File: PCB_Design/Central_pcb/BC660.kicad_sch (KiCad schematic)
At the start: 26 parts, among them J1 SMA_CONNECTOR, J2 Conn_01x01_Pin, J3 Conn_01x02_Pin, J4 SIM8051-6-0-14-01-X-REVD, J5 Conn_01x02_Pin, J6 Conn_01x06_Pin, U1 BC660K-GL, U2 ESDS304DBVR

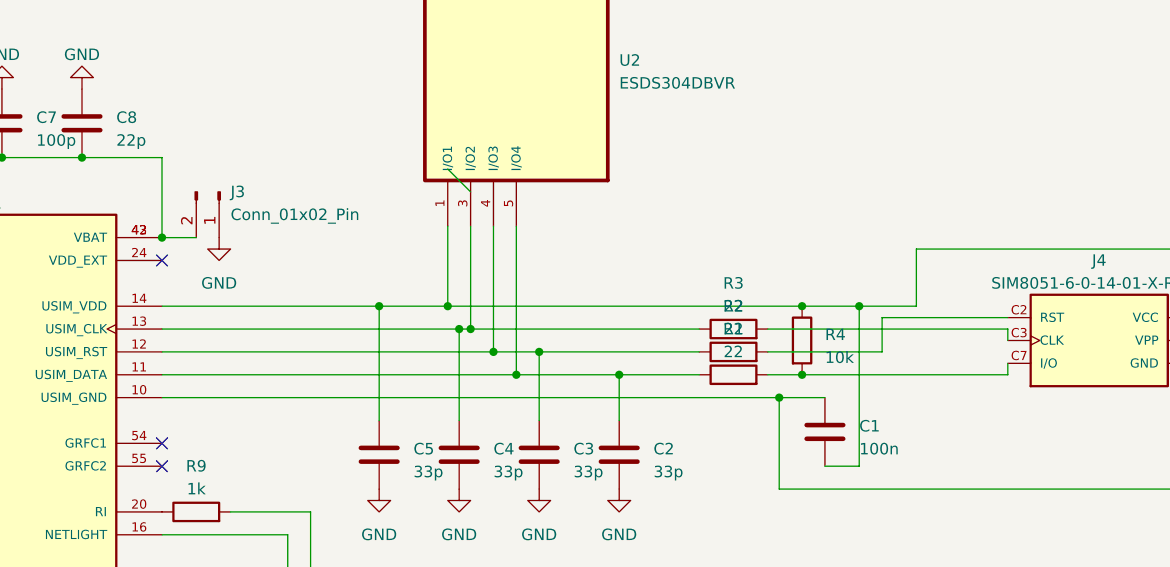
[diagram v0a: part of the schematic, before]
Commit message: Power part added
Power part is finished with power footprints
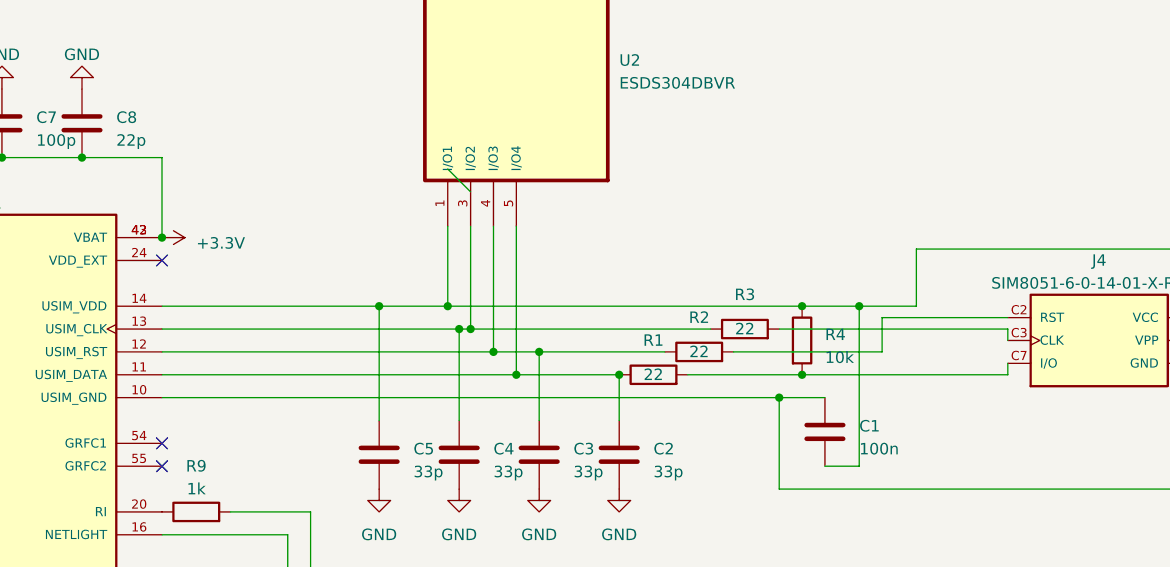
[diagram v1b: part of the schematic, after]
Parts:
- removed J3: Conn_01x02_Pin, Connector_PinHeader_2.54mm:PinHeader_1x02_P2.54mm_Vertical, symbol Connector:Conn_01x02_Pin
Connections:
- net +3.3V: now reaches C6.2, C7.2, C8.2, C9.2, U1.42 (VBAT), U1.43 (VBAT)
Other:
- moved on the sheet: R1, R2, R3
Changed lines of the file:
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@@
   (junction (at 124.46 66.04) (diameter 0) (color 0 0 0 0)
   )
+  (junction (at 184.15 90.17) (diameter 0) (color 0 0 0 0)
+  )
+  (junction (at 166.37 85.09) (diameter 0) (color 0 0 0 0)
+  )
+  (junction (at 175.26 87.63) (diameter 0) (color 0 0 0 0)
+  )
+  (junction (at 210.82 82.55) (diameter 0) (color 0 0 0 0)
+  )
+  (junction (at 165.1 82.55) (diameter 0) (color 0 0 0 0)
+  )
   (junction (at 133.35 74.93) (diameter 0) (color 0 0 0 0)
-  )
-  (junction (at 184.15 90.17) (diameter 0) (color 0 0 0 0)
-  )
-  (junction (at 166.37 85.09) (diameter 0) (color 0 0 0 0)
-  )
-  (junction (at 175.26 87.63) (diameter 0) (color 0 0 0 0)
-  )
-  (junction (at 210.82 82.55) (diameter 0) (color 0 0 0 0)
-  )
-  (junction (at 165.1 82.55) (diameter 0) (color 0 0 0 0)
   )
   (junction (at 167.64 85.09) (diameter 0) (color 0 0 0 0)
@@
     (stroke (width 0) (type default))
   )
-  (wire (pts (xy 133.35 74.93) (xy 137.16 74.93))
-    (stroke (width 0) (type default))
-  )
   (wire (pts (xy 58.42 97.79) (xy 53.34 97.79))
     (stroke (width 0) (type default))
@@
     (stroke (width 0) (type default))
   )
-  (wire (pts (xy 200.66 90.17) (xy 204.47 90.17))
+  (wire (pts (xy 191.77 90.17) (xy 204.47 90.17))
     (stroke (width 0) (type default))
   )
@@
     (stroke (width 0) (type default))
   )
-  (wire (pts (xy 167.64 85.09) (xy 193.04 85.09))
+  (wire (pts (xy 167.64 85.09) (xy 194.31 85.09))
     (stroke (width 0) (type default))
   )
@@
     (stroke (width 0) (type default))
   )
-  (wire (pts (xy 200.66 85.09) (xy 227.33 85.09))
+  (wire (pts (xy 201.93 85.09) (xy 227.33 85.09))
     (stroke (width 0) (type default))
   )
@@
     (stroke (width 0) (type default))
   )
-  (wire (pts (xy 200.66 87.63) (xy 213.36 87.63))
+  (wire (pts (xy 196.85 87.63) (xy 213.36 87.63))
     (stroke (width 0) (type default))
   )
@@
     (stroke (width 0) (type default))
   )
-  (wire (pts (xy 184.15 90.17) (xy 193.04 90.17))
-    (stroke (width 0) (type default))
-  )
   (wire (pts (xy 53.34 102.87) (xy 73.66 102.87))
     (stroke (width 0) (type default))
@@
     (stroke (width 0) (type default))
   )
-  (wire (pts (xy 175.26 87.63) (xy 193.04 87.63))
+  (wire (pts (xy 175.26 87.63) (xy 189.23 87.63))
     (stroke (width 0) (type default))
   )
@@
     )
   )
-  (symbol (lib_id "Device:R") (at 196.85 85.09 90) (unit 1)
-    (in_bom yes) (on_board yes) (dnp no) (fields_autoplaced)
-    (property "Reference" "R3" (at 196.85 80.01 90)
-      (effects (font (size 1.27 1.27)))
-    )
-    (property "Value" "22" (at 196.85 82.55 90)
-      (effects (font (size 1.27 1.27)))
-    )
-    (property "Footprint" "Resistor_SMD:R_0805_2012Metric_Pad1.20x1.40mm_HandSolder" (at 196.85 86.868 90)
-      (effects (font (size 1.27 1.27)) hide)
-    )
-    (property "Datasheet" "~" (at 196.85 85.09 0)
+  (symbol (lib_id "Device:R") (at 198.12 85.09 90) (unit 1)
+    (in_bom yes) (on_board yes) (dnp no)
+    (property "Reference" "R3" (at 198.12 81.28 90)
+      (effects (font (size 1.27 1.27)))
+    )
+    (property "Value" "22" (at 198.12 85.09 90)
+      (effects (font (size 1.27 1.27)))
+    )
+    (property "Footprint" "Resistor_SMD:R_0805_2012Metric_Pad1.20x1.40mm_HandSolder" (at 198.12 86.868 90)
+      (effects (font (size 1.27 1.27)) hide)
+    )
+    (property "Datasheet" "~" (at 198.12 85.09 0)
       (effects (font (size 1.27 1.27)) hide)
     )
@@
         (path "/d627ecd8-d3ea-468a-86f8-a115d49eee0e"
           (reference "C2") (unit 1)
-        )
-      )
-    )
-  )
-  (symbol (lib_id "power:GND") (at 139.7 74.93 0) (unit 1)
-    (in_bom yes) (on_board yes) (dnp no) (fields_autoplaced)
-    (property "Reference" "#PWR08" (at 139.7 81.28 0)
-      (effects (font (size 1.27 1.27)) hide)
-    )
-    (property "Value" "GND" (at 139.7 80.01 0)
-      (effects (font (size 1.27 1.27)))
-    )
-    (property "Footprint" "" (at 139.7 74.93 0)
-      (effects (font (size 1.27 1.27)) hide)
-    )
-    (property "Datasheet" "" (at 139.7 74.93 0)
-      (effects (font (size 1.27 1.27)) hide)
-    )
-    (pin "1")
-    (instances
-      (project "Central_pcb"
-        (path "/4d244925-fc91-48ed-8daa-e4f0d6afeb7f"
-          (reference "#PWR08") (unit 1)
-        )
-        (path "/4d244925-fc91-48ed-8daa-e4f0d6afeb7f/a01f4f1b-67d6-4452-bfd1-ae36b9ad65e8"
-          (reference "#PWR08") (unit 1)
-        )
-      )
-      (project "bc660_breakoutboard"
-        (path "/d627ecd8-d3ea-468a-86f8-a115d49eee0e"
-          (reference "#PWR08") (unit 1)
         )
       )
@@
     )
   )
+  (symbol (lib_id "power:+3.3V") (at 133.35 74.93 270) (unit 1)
+    (in_bom yes) (on_board yes) (dnp no) (fields_autoplaced)
+    (property "Reference" "#PWR08" (at 129.54 74.93 0)
+      (effects (font (size 1.27 1.27)) hide)
+    )
+    (property "Value" "+3.3V" (at 137.16 75.565 90)
+      (effects (font (size 1.27 1.27)) (justify left))
+    )
+    (property "Footprint" "" (at 133.35 74.93 0)
+      (effects (font (size 1.27 1.27)) hide)
+    )
+    (property "Datasheet" "" (at 133.35 74.93 0)
+      (effects (font (size 1.27 1.27)) hide)
+    )
+    (pin "1")
+    (instances
+      (project "Central_pcb"
+        (path "/4d244925-fc91-48ed-8daa-e4f0d6afeb7f/a01f4f1b-67d6-4452-bfd1-ae36b9ad65e8"
+          (reference "#PWR08") (unit 1)
+        )
+      )
+    )
+  )
   (symbol (lib_id "power:GND") (at 97.79 58.42 180) (unit 1)
     (in_bom yes) (on_board yes) (dnp no) (fields_autoplaced)
@@
     )
   )
-  (symbol (lib_id "Device:R") (at 196.85 90.17 90) (unit 1)
-    (in_bom yes) (on_board yes) (dnp no) (fields_autoplaced)
-    (property "Reference" "R1" (at 196.85 85.09 90)
-      (effects (font (size 1.27 1.27)))
-    )
-    (property "Value" "22" (at 196.85 87.63 90)
-      (effects (font (size 1.27 1.27)))
-    )
-    (property "Footprint" "Resistor_SMD:R_0805_2012Metric_Pad1.20x1.40mm_HandSolder" (at 196.85 91.948 90)
-      (effects (font (size 1.27 1.27)) hide)
-    )
-    (property "Datasheet" "~" (at 196.85 90.17 0)
+  (symbol (lib_id "Device:R") (at 187.96 90.17 90) (unit 1)
+    (in_bom yes) (on_board yes) (dnp no)
+    (property "Reference" "R1" (at 187.96 86.36 90)
+      (effects (font (size 1.27 1.27)))
+    )
+    (property "Value" "22" (at 187.96 90.17 90)
+      (effects (font (size 1.27 1.27)))
+    )
+    (property "Footprint" "Resistor_SMD:R_0805_2012Metric_Pad1.20x1.40mm_HandSolder" (at 187.96 91.948 90)
+      (effects (font (size 1.27 1.27)) hide)
+    )
+    (property "Datasheet" "~" (at 187.96 90.17 0)
       (effects (font (size 1.27 1.27)) hide)
     )
@@
         (path "/d627ecd8-d3ea-468a-86f8-a115d49eee0e"
           (reference "R1") (unit 1)
-        )
-      )
-    )
-  )
-  (symbol (lib_id "Connector:Conn_01x02_Pin") (at 139.7 69.85 270) (unit 1)
-    (in_bom yes) (on_board yes) (dnp no) (fields_autoplaced)
-    (property "Reference" "J3" (at 140.97 69.85 90)
-      (effects (font (size 1.27 1.27)) (justify left))
-    )
-    (property "Value" "Conn_01x02_Pin" (at 140.97 72.39 90)
-      (effects (font (size 1.27 1.27)) (justify left))
-    )
-    (property "Footprint" "Connector_PinHeader_2.54mm:PinHeader_1x02_P2.54mm_Vertical" (at 139.7 69.85 0)
-      (effects (font (size 1.27 1.27)) hide)
-    )
-    (property "Datasheet" "~" (at 139.7 69.85 0)
-      (effects (font (size 1.27 1.27)) hide)
-    )
-    (pin "1")
-    (pin "2")
-    (instances
-      (project "Central_pcb"
-        (path "/4d244925-fc91-48ed-8daa-e4f0d6afeb7f"
-          (reference "J3") (unit 1)
-        )
-        (path "/4d244925-fc91-48ed-8daa-e4f0d6afeb7f/a01f4f1b-67d6-4452-bfd1-ae36b9ad65e8"
-          (reference "J5") (unit 1)
-        )
-      )
-      (project "bc660_breakoutboard"
-        (path "/d627ecd8-d3ea-468a-86f8-a115d49eee0e"
-          (reference "J3") (unit 1)
         )
       )
@@
     )
   )
-  (symbol (lib_id "Device:R") (at 196.85 87.63 90) (unit 1)
-    (in_bom yes) (on_board yes) (dnp no) (fields_autoplaced)
-    (property "Reference" "R2" (at 196.85 82.55 90)
-      (effects (font (size 1.27 1.27)))
-    )
-    (property "Value" "22" (at 196.85 85.09 90)
-      (effects (font (size 1.27 1.27)))
-    )
-    (property "Footprint" "Resistor_SMD:R_0805_2012Metric_Pad1.20x1.40mm_HandSolder" (at 196.85 89.408 90)
-      (effects (font (size 1.27 1.27)) hide)
-    )
-    (property "Datasheet" "~" (at 196.85 87.63 0)
-      (effects (font (size 1.27 1.27)) hide)
-    )
+  (symbol (lib_id "Device:R") (at 193.04 87.63 90) (unit 1)
+    (in_bom yes) (on_board yes) (dnp no)
+    (property "Reference" "R2" (at 193.04 83.82 90)
+      (effects (font (size 1.27 1.27)))
+    )
+    (property "Value" "22" (at 193.04 87.63 90)
+      (effects (font (size 1.27 1.27)))
+    )
+    (property "Footprint" "Resistor_SMD:R_0805_2012Metric_Pad1.20x1.40mm_HandSolder" (at 193.04 89.408 90)
+      (effects (font (size 1.27 1.27)) hide)
+    )
+    (property "Datasheet" "~" (at 193.04 87.63 0)
+      (effects (font (size 1.27 1.27)) hide)
+    )

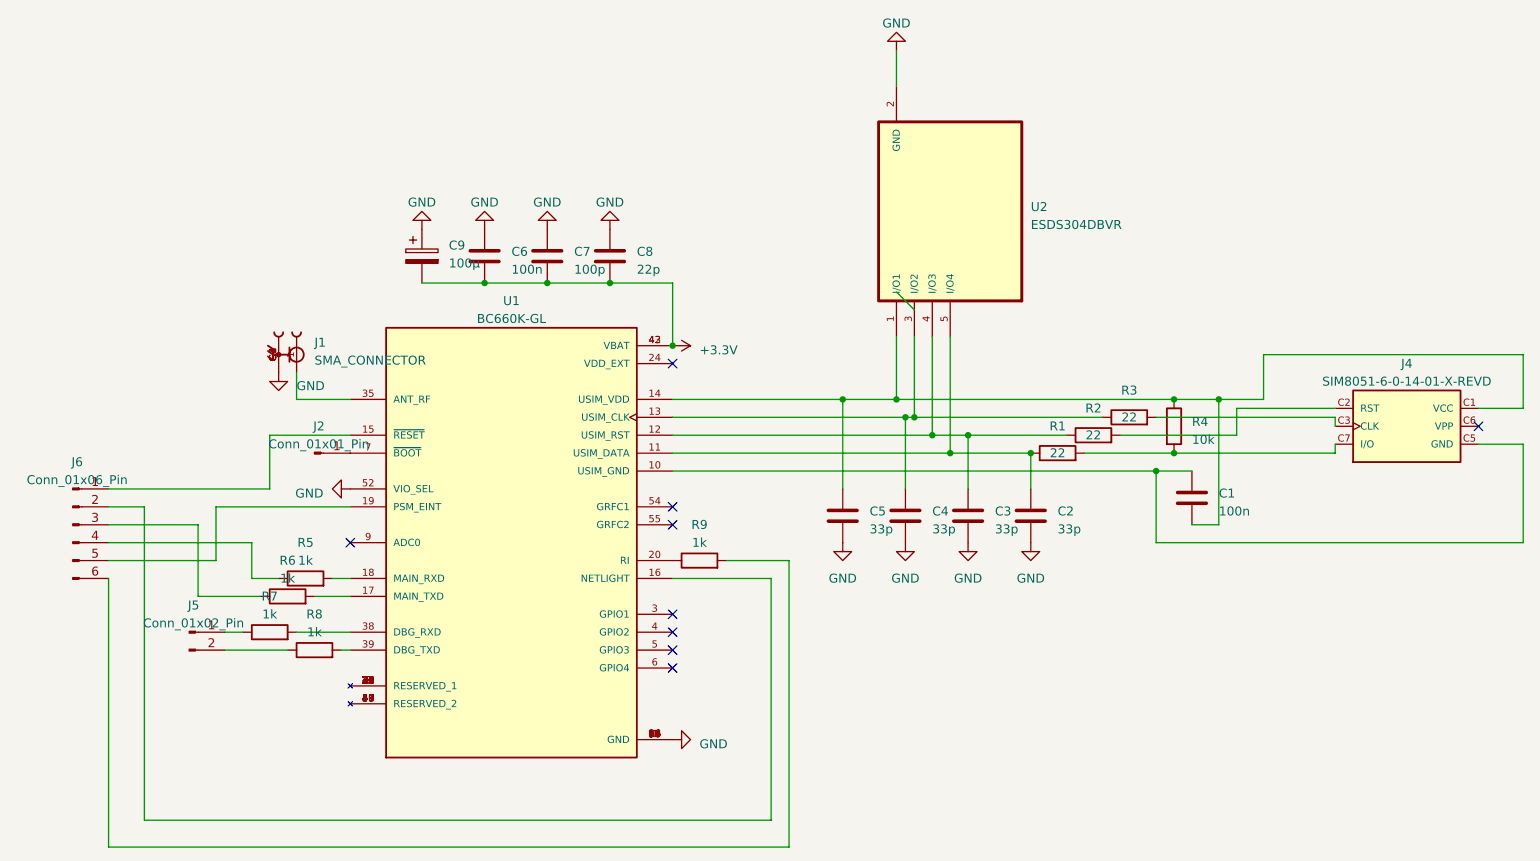
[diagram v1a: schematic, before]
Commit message: Scematic update
update scematic and added some footrpints
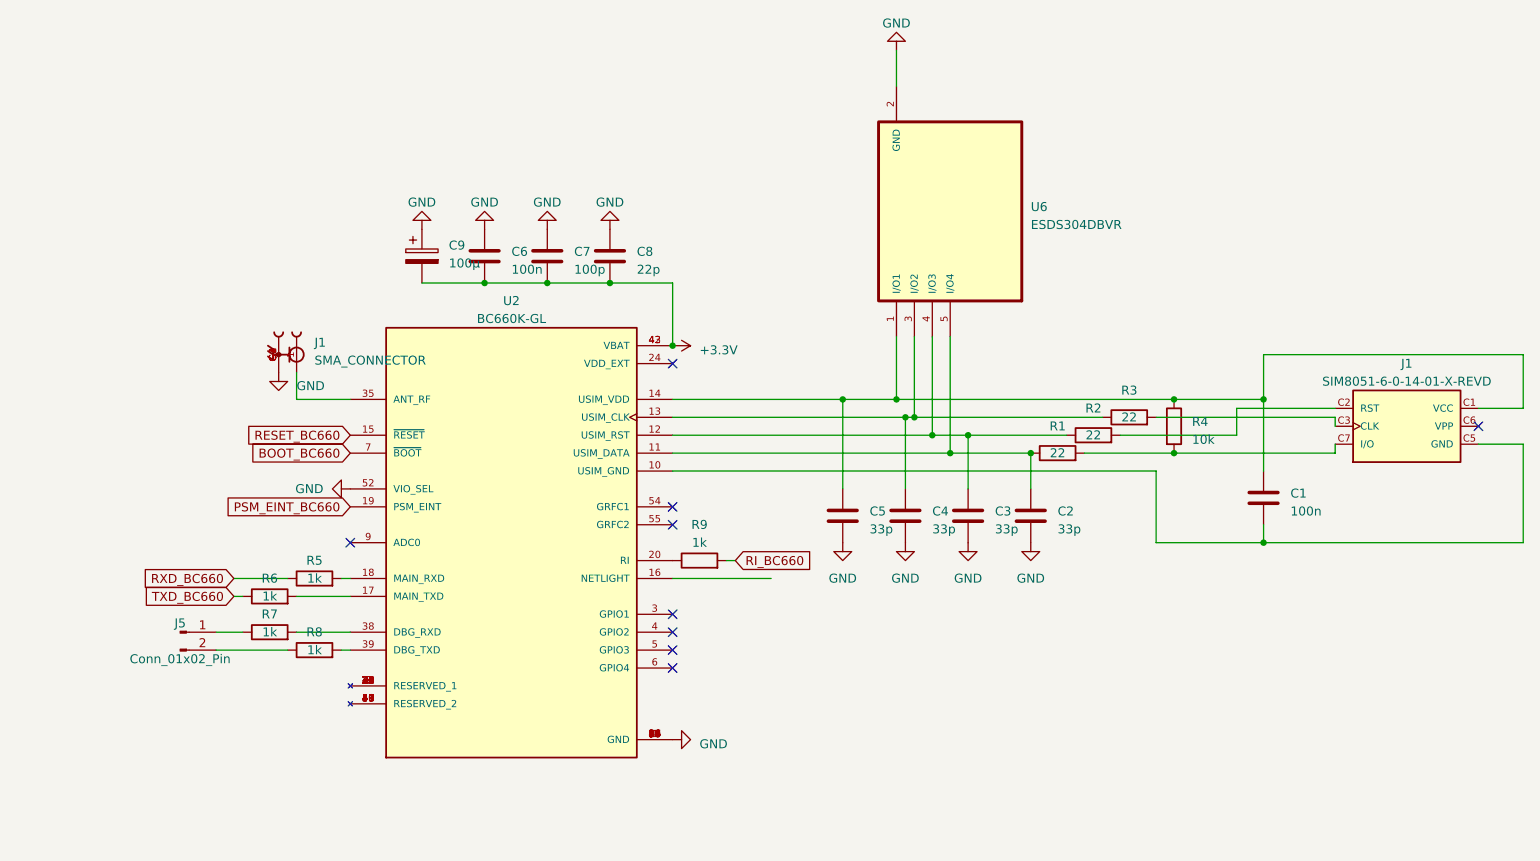
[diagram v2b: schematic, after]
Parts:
- removed J2: Conn_01x01_Pin, Connector_PinHeader_2.54mm:PinHeader_1x01_P2.54mm_Vertical, symbol Connector:Conn_01x01_Pin
- removed J4: SIM8051-6-0-14-01-X-REVD, SIM8051-6-0-14-01-X-REVD:GCT_SIM8051-6-0-14-01-X-REVD, symbol SIM8051-6-0-14-01-X-REVD:SIM8051-6-0-14-01-X-REVD
- removed J6: Conn_01x06_Pin, Connector_PinHeader_2.54mm:PinHeader_1x06_P2.54mm_Vertical, symbol Connector:Conn_01x06_Pin
- removed U1: BC660K-GL, BC660K-GL:XCVR_BC660K-GL, symbol BC660K-GL:BC660K-GL
- removed U2: ESDS304DBVR, ESDS304DBVR:SOT95P280X145-5N, symbol ESDS304DBVR:ESDS304DBVR
- added J1: SIM8051-6-0-14-01-X-REVD, Central:GCT_SIM8051-6-0-14-01-X-REVD, symbol SIM8051:SIM8051-6-0-14-01-X-REVD
- added U2: BC660K-GL, Central:XCVR_BC660K-GL, symbol BC660:BC660K-GL
- added U6: ESDS304DBVR, Central:SOT95P280X145-5N, symbol ESDS304:ESDS304DBVR
- J1: footprint SMA_CONNECTOR:LPRS_SMA_CONNECTOR -> Central:LPRS_SMA_CONNECTOR
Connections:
- net +3.3V: now also U2.42 (VBAT), U2.43 (VBAT)
- net GND: now also U2.1 (GND), U2.27 (GND), U2.34 (GND), U2.36 (GND), U2.37 (GND), U2.40 (GND), U2.41 (GND), U2.52 (VIO_SEL), U2.56 (GND), U2.57 (GND), U2.58 (GND), U6.2 (GND)
- net TXD_BC660: now reaches R6.1
- net RXD_BC660: now reaches R5.1
- net RI_BC660: now reaches R9.2
- net at C4.1, R3.1: now also U2.13 (USIM_CLK), U6.3 (I/O2)
- net at R3.2: now also J1.C3 (CLK)
- net at C1.2, C5.1, R4.1: now also J1.C1 (VCC), U2.14 (USIM_VDD), U6.1 (I/O1)
- net at R1.2, R4.2: now also J1.C7 (I/O)
- net at C2.1, R1.1: now also U2.11 (USIM_DATA), U6.5 (I/O4)
- net at R6.2: now also U2.17 (MAIN_TXD)
- net at J1.1: now also U2.35 (ANT_RF)
- net at R7.2: now also U2.38 (DBG_RXD)
- net at R5.2: now also U2.18 (MAIN_RXD)
- net at C3.1, R2.1: now also U2.12 (USIM_RST), U6.4 (I/O3)
- net at C1.1: now also J1.C5 (GND), U2.10 (USIM_GND)
- net at R8.2: now also U2.39 (DBG_TXD)
- net at R9.1: now also U2.20 (RI)
- net at R2.2: now also J1.C2 (RST)
- new net: U2.2 (RESERVED_1), U2.21 (RESERVED_1), U2.22 (RESERVED_1), U2.23 (RESERVED_1), U2.25 (RESERVED_1), U2.26 (RESERVED_1), U2.28 (RESERVED_1), U2.29 (RESERVED_1), U2.30 (RESERVED_1), U2.31 (RESERVED_1), U2.32 (RESERVED_1), U2.33 (RESERVED_1), U2.44 (RESERVED_1), U2.45 (RESERVED_1), U2.8 (RESERVED_1)
- new net: U2.46 (RESERVED_2), U2.47 (RESERVED_2), U2.48 (RESERVED_2), U2.49 (RESERVED_2), U2.50 (RESERVED_2), U2.51 (RESERVED_2), U2.53 (RESERVED_2)
- new net BOOT_BC660: U2.7 (~{BOOT})
- new net PSM_EINT_BC660: U2.19 (PSM_EINT)
- new net RESET_BC660: U2.15 (~{RESET})
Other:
- moved on the sheet: C1, J5, R5, R6
